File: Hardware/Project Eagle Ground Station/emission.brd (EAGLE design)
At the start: 74.9 x 152.1 mm, 23 parts

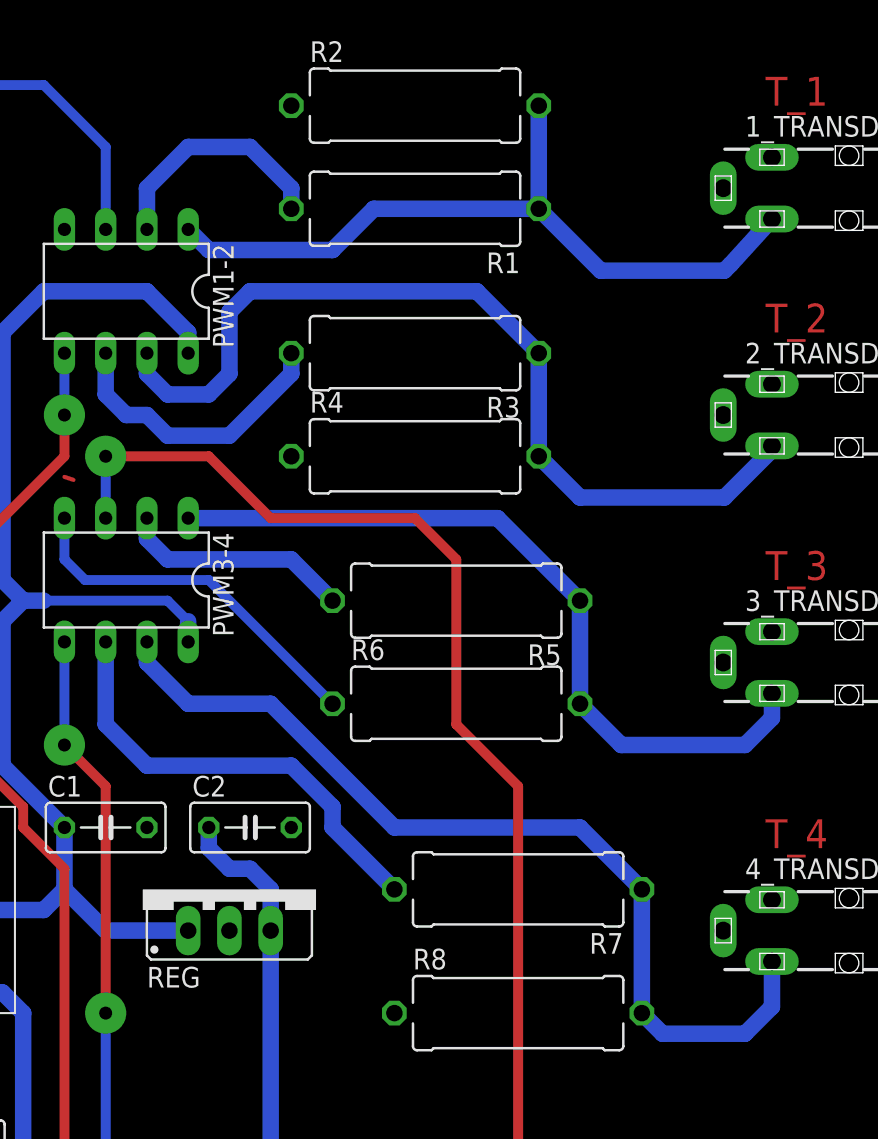
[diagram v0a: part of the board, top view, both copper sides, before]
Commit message: Correct the AOP connection
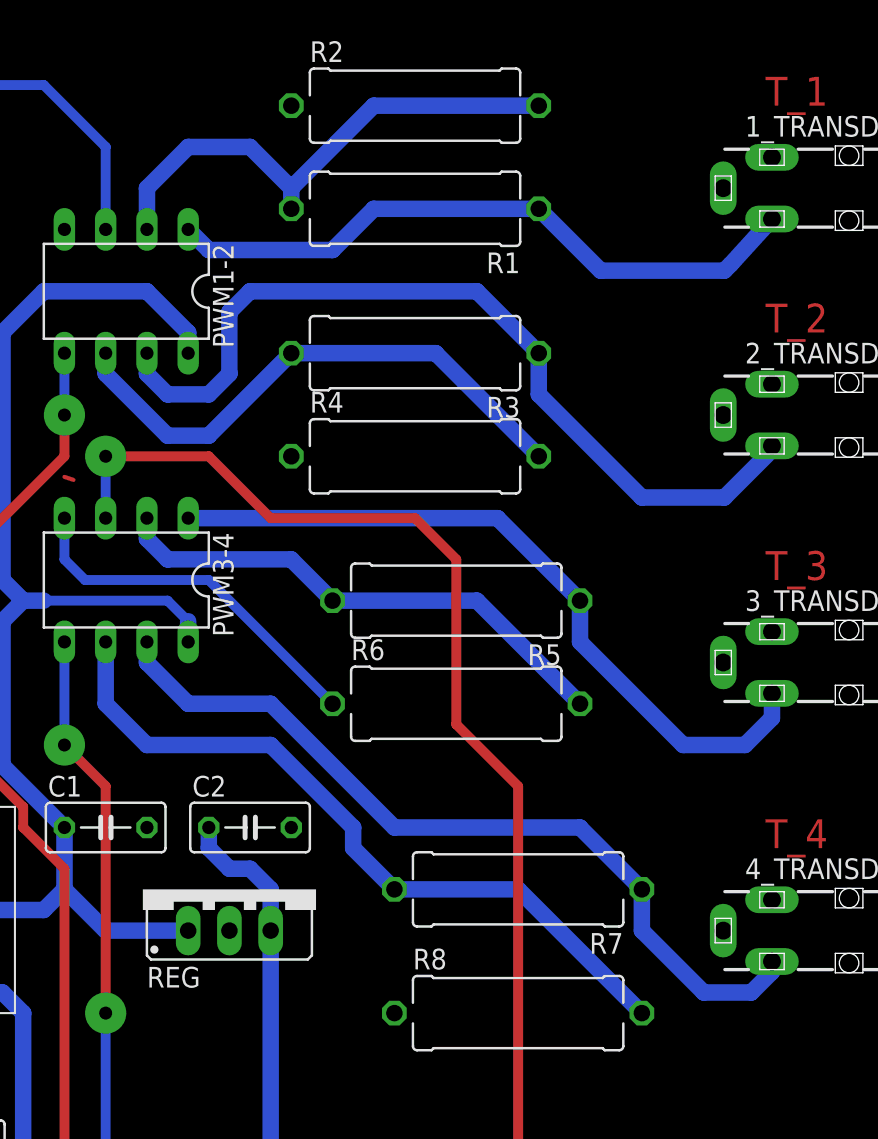
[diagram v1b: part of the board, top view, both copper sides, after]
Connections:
- net IN1: no longer R2.2
- net IN2: no longer R4.2
- net IN3: no longer R6.2
- net IN4: no longer R8.2
- net N$1: now also R2.2
- net N$2: now also R4.2
- net N$4: now also R6.2
- net N$5: now also R8.2
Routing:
- net N$4: track 14.3 -> 32.1 mm
- net N$5: track 27.8 -> 45.5 mm
- net N$1: track 14.8 -> 32.1 mm
- net N$2: track 17.9 -> 34.3 mm
- net IN1: track 46.9 -> 40.5 mm
- net IN4: track 57.2 -> 50.8 mm
- net IN3: track 47.7 -> 45.4 mm
- net IN2: track 55.6 -> 53.4 mm
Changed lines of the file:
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@@
 <layer number="23" name="tOrigins" color="15" fill="1" visible="yes" active="yes"/>
 <layer number="24" name="bOrigins" color="15" fill="1" visible="yes" active="yes"/>
-<layer number="25" name="tNames" color="7" fill="1" visible="yes" active="yes"/>
-<layer number="26" name="bNames" color="7" fill="1" visible="yes" active="yes"/>
-<layer number="27" name="tValues" color="7" fill="1" visible="yes" active="yes"/>
-<layer number="28" name="bValues" color="7" fill="1" visible="yes" active="yes"/>
-<layer number="29" name="tStop" color="7" fill="3" visible="yes" active="yes"/>
-<layer number="30" name="bStop" color="7" fill="6" visible="yes" active="yes"/>
+<layer number="25" name="tNames" color="7" fill="1" visible="no" active="yes"/>
+<layer number="26" name="bNames" color="7" fill="1" visible="no" active="yes"/>
+<layer number="27" name="tValues" color="7" fill="1" visible="no" active="yes"/>
+<layer number="28" name="bValues" color="7" fill="1" visible="no" active="yes"/>
+<layer number="29" name="tStop" color="7" fill="3" visible="no" active="yes"/>
+<layer number="30" name="bStop" color="7" fill="6" visible="no" active="yes"/>
 <layer number="31" name="tCream" color="7" fill="4" visible="yes" active="yes"/>
 <layer number="32" name="bCream" color="7" fill="5" visible="yes" active="yes"/>
@@
 <contactref element="PWM1-2" pad="1"/>
 <contactref element="1_TRANSDUCER" pad="3"/>
-<contactref element="R1" pad="1"/>
-<contactref element="R2" pad="2"/>
 <wire x1="28.33" y1="114.94" x2="25.79" y2="112.15" width="1.016" layer="16"/>
 <wire x1="25.79" y1="112.15" x2="25.4" y2="111.76" width="1.016" layer="16"/>
 <wire x1="25.4" y1="111.76" x2="17.78" y2="111.76" width="1.016" layer="16"/>
-<wire x1="17.78" y1="111.76" x2="13.97" y2="115.57" width="1.016" layer="16"/>
-<wire x1="13.97" y1="121.92" x2="13.97" y2="115.57" width="1.016" layer="16"/>
-<wire x1="13.97" y1="115.57" x2="3.81" y2="115.57" width="1.016" layer="16"/>
 <wire x1="3.81" y1="115.57" x2="1.27" y2="113.03" width="1.016" layer="16"/>
 <wire x1="1.27" y1="113.03" x2="-6.35" y2="113.03" width="1.016" layer="16"/>
 <wire x1="-6.35" y1="113.03" x2="-7.62" y2="114.3" width="1.016" layer="16"/>
+<contactref element="R1" pad="1"/>
+<wire x1="3.81" y1="115.57" x2="13.97" y2="115.57" width="1.016" layer="16"/>
+<wire x1="13.97" y1="115.57" x2="17.78" y2="111.76" width="1.016" layer="16"/>
 </signal>
 <signal name="V+">
@@
 <contactref element="PWM1-2" pad="7"/>
 <contactref element="2_TRANSDUCER" pad="3"/>
-<contactref element="R3" pad="1"/>
-<contactref element="R4" pad="2"/>
 <wire x1="28.33" y1="100.97" x2="28.33" y2="100.72" width="1.016" layer="16"/>
 <wire x1="28.33" y1="100.72" x2="25.4" y2="97.79" width="1.016" layer="16"/>
-<wire x1="25.4" y1="97.79" x2="16.51" y2="97.79" width="1.016" layer="16"/>
-<wire x1="16.51" y1="97.79" x2="13.97" y2="100.33" width="1.016" layer="16"/>
-<wire x1="13.97" y1="100.33" x2="13.97" y2="106.68" width="1.016" layer="16"/>
+<wire x1="25.4" y1="97.79" x2="20.32" y2="97.79" width="1.016" layer="16"/>
 <wire x1="-10.16" y1="106.68" x2="-10.16" y2="105.41" width="1.016" layer="16"/>
 <wire x1="-10.16" y1="105.41" x2="-8.89" y2="104.14" width="1.016" layer="16"/>
@@
 <wire x1="-5.08" y1="109.22" x2="-3.81" y2="110.49" width="1.016" layer="16"/>
 <wire x1="-3.81" y1="110.49" x2="10.16" y2="110.49" width="1.016" layer="16"/>
+<contactref element="R3" pad="1"/>
 <wire x1="10.16" y1="110.49" x2="13.97" y2="106.68" width="1.016" layer="16"/>
+<wire x1="13.97" y1="106.68" x2="13.97" y2="104.14" width="1.016" layer="16"/>
+<wire x1="13.97" y1="104.14" x2="20.32" y2="97.79" width="1.016" layer="16"/>
 </signal>
 <signal name="IN3">
 <contactref element="PWM3-4" pad="1"/>
 <contactref element="3_TRANSDUCER" pad="3"/>
-<contactref element="R6" pad="2"/>
-<contactref element="R5" pad="1"/>
 <wire x1="28.33" y1="85.73" x2="28.33" y2="84.21" width="1.016" layer="16"/>
 <wire x1="28.33" y1="84.21" x2="26.67" y2="82.55" width="1.016" layer="16"/>
-<wire x1="26.67" y1="82.55" x2="19.05" y2="82.55" width="1.016" layer="16"/>
-<wire x1="19.05" y1="82.55" x2="16.51" y2="85.09" width="1.016" layer="16"/>
-<wire x1="16.51" y1="85.09" x2="16.51" y2="91.44" width="1.016" layer="16"/>
+<wire x1="26.67" y1="82.55" x2="22.86" y2="82.55" width="1.016" layer="16"/>
 <wire x1="-7.62" y1="96.52" x2="11.43" y2="96.52" width="1.016" layer="16"/>
+<contactref element="R5" pad="1"/>
 <wire x1="11.43" y1="96.52" x2="16.51" y2="91.44" width="1.016" layer="16"/>
+<wire x1="16.51" y1="91.44" x2="16.51" y2="88.9" width="1.016" layer="16"/>
+<wire x1="16.51" y1="88.9" x2="22.86" y2="82.55" width="1.016" layer="16"/>
 </signal>
 <signal name="IN4">
 <contactref element="PWM3-4" pad="7"/>
 <contactref element="4_TRANSDUCER" pad="3"/>
-<contactref element="R7" pad="1"/>
-<contactref element="R8" pad="2"/>
-<wire x1="28.33" y1="69.22" x2="28.33" y2="66.43" width="1.016" layer="16"/>
-<wire x1="28.33" y1="66.43" x2="26.67" y2="64.77" width="1.016" layer="16"/>
-<wire x1="26.67" y1="64.77" x2="21.59" y2="64.77" width="1.016" layer="16"/>
-<wire x1="21.59" y1="64.77" x2="20.32" y2="66.04" width="1.016" layer="16"/>
-<wire x1="20.32" y1="73.66" x2="20.32" y2="66.04" width="1.016" layer="16"/>
-<wire x1="20.32" y1="73.66" x2="16.51" y2="77.47" width="1.016" layer="16"/>
+<wire x1="28.33" y1="69.22" x2="28.33" y2="68.58" width="1.016" layer="16"/>
 <wire x1="16.51" y1="77.47" x2="5.08" y2="77.47" width="1.016" layer="16"/>
 <wire x1="5.08" y1="77.47" x2="-2.54" y2="85.09" width="1.016" layer="16"/>
@@
 <wire x1="-7.62" y1="85.09" x2="-10.16" y2="87.63" width="1.016" layer="16"/>
 <wire x1="-10.16" y1="87.63" x2="-10.16" y2="88.9" width="1.016" layer="16"/>
+<contactref element="R7" pad="1"/>
+<wire x1="16.51" y1="77.47" x2="20.32" y2="73.66" width="1.016" layer="16"/>
+<wire x1="20.32" y1="73.66" x2="20.32" y2="71.12" width="1.016" layer="16"/>
+<wire x1="20.32" y1="71.12" x2="24.13" y2="67.31" width="1.016" layer="16"/>
+<wire x1="24.13" y1="67.31" x2="27.06" y2="67.31" width="1.016" layer="16"/>
+<wire x1="27.06" y1="67.31" x2="28.33" y2="68.58" width="1.016" layer="16"/>
 </signal>
 <signal name="PWM1">
@@
 <wire x1="-7.62" y1="119.38" x2="-10.16" y2="116.84" width="1.016" layer="16"/>
 <wire x1="-10.16" y1="116.84" x2="-10.16" y2="114.3" width="1.016" layer="16"/>
+<contactref element="R2" pad="2"/>
+<wire x1="13.97" y1="121.92" x2="3.81" y2="121.92" width="1.016" layer="16"/>
+<wire x1="3.81" y1="121.92" x2="-1.27" y2="116.84" width="1.016" layer="16"/>
+</signal>
+<signal name="N$6">
+<wire x1="-15.24" y1="99.06" x2="-14.683884375" y2="98.874540625" width="0.254" layer="1"/>
 </signal>
 <signal name="N$2">
+<contactref element="R3" pad="2"/>
+<contactref element="R4" pad="2"/>
 <contactref element="PWM1-2" pad="6"/>
-<contactref element="R3" pad="2"/>
-<wire x1="-1.27" y1="106.68" x2="-1.27" y2="105.41" width="1.016" layer="16"/>
-<wire x1="-12.7" y1="104.14" x2="-12.7" y2="106.68" width="1.016" layer="16"/>
-<wire x1="-12.7" y1="104.14" x2="-11.43" y2="102.87" width="1.016" layer="16"/>
-<wire x1="-11.43" y1="102.87" x2="-10.16" y2="102.87" width="1.016" layer="16"/>
-<wire x1="-10.16" y1="102.87" x2="-8.89" y2="101.6" width="1.016" layer="16"/>
-<wire x1="-8.89" y1="101.6" x2="-5.08" y2="101.6" width="1.016" layer="16"/>
-<wire x1="-5.08" y1="101.6" x2="-1.27" y2="105.41" width="1.016" layer="16"/>
+<wire x1="-12.7" y1="106.68" x2="-12.7" y2="105.41" width="1.016" layer="16"/>
+<wire x1="-12.7" y1="105.41" x2="-8.89" y2="101.6" width="1.016" layer="16"/>
+<wire x1="-8.89" y1="101.6" x2="-6.35" y2="101.6" width="1.016" layer="16"/>
+<wire x1="-6.35" y1="101.6" x2="-1.27" y2="106.68" width="1.016" layer="16"/>
+<wire x1="-1.27" y1="106.68" x2="7.62" y2="106.68" width="1.016" layer="16"/>
+<wire x1="7.62" y1="106.68" x2="13.97" y2="100.33" width="1.016" layer="16"/>
 </signal>
 <signal name="N$4">
+<contactref element="R5" pad="2"/>
+<contactref element="R6" pad="2"/>
 <contactref element="PWM3-4" pad="2"/>
-<contactref element="R5" pad="2"/>
 <wire x1="-10.16" y1="96.52" x2="-10.16" y2="95.25" width="1.016" layer="16"/>
 <wire x1="-10.16" y1="95.25" x2="-8.89" y2="93.98" width="1.016" layer="16"/>
 <wire x1="-8.89" y1="93.98" x2="-1.27" y2="93.98" width="1.016" layer="16"/>
 <wire x1="-1.27" y1="93.98" x2="1.27" y2="91.44" width="1.016" layer="16"/>
+<wire x1="1.27" y1="91.44" x2="10.16" y2="91.44" width="1.016" layer="16"/>
+<wire x1="10.16" y1="91.44" x2="16.51" y2="85.09" width="1.016" layer="16"/>
 </signal>
 <signal name="N$5">
 <contactref element="PWM3-4" pad="6"/>
 <contactref element="R7" pad="2"/>
-<wire x1="-12.7" y1="88.9" x2="-12.7" y2="83.82" width="1.016" layer="16"/>
-<wire x1="-12.7" y1="83.82" x2="-10.16" y2="81.28" width="1.016" layer="16"/>
-<wire x1="-10.16" y1="81.28" x2="-1.27" y2="81.28" width="1.016" layer="16"/>
-<wire x1="-1.27" y1="81.28" x2="1.27" y2="78.74" width="1.016" layer="16"/>
-<wire x1="1.27" y1="78.74" x2="1.27" y2="77.47" width="1.016" layer="16"/>
-<wire x1="1.27" y1="77.47" x2="5.08" y2="73.66" width="1.016" layer="16"/>
-</signal>
-<signal name="N$6">
-<wire x1="-15.24" y1="99.06" x2="-14.683884375" y2="98.874540625" width="0.254" layer="1"/>
+<contactref element="R8" pad="2"/>
+<wire x1="-12.7" y1="88.9" x2="-12.7" y2="85.09" width="1.016" layer="16"/>
+<wire x1="-12.7" y1="85.09" x2="-10.16" y2="82.55" width="1.016" layer="16"/>
+<wire x1="-10.16" y1="82.55" x2="-2.54" y2="82.55" width="1.016" layer="16"/>
+<wire x1="-2.54" y1="82.55" x2="2.54" y2="77.47" width="1.016" layer="16"/>
+<wire x1="2.54" y1="77.47" x2="2.54" y2="76.2" width="1.016" layer="16"/>
+<wire x1="2.54" y1="76.2" x2="5.08" y2="73.66" width="1.016" layer="16"/>
+<wire x1="5.08" y1="73.66" x2="12.7" y2="73.66" width="1.016" layer="16"/>
+<wire x1="12.7" y1="73.66" x2="20.32" y2="66.04" width="1.016" layer="16"/>
 </signal>
 </signals>
